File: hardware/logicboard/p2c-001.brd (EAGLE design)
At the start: 89 x 51 mm, 53 parts, among them IC1 74LS06N, J1 MKR, J11 Qwiic, J2 GPIO, J3 9V, J4 RLY, J5 SPI, J6 DIN5, J7 DIN5, K1 G5V1, Q11 220mA/50V/3.5Ω, Q12 220mA/50V/3.5Ω, T1 2SC1815, U1 DS18B20

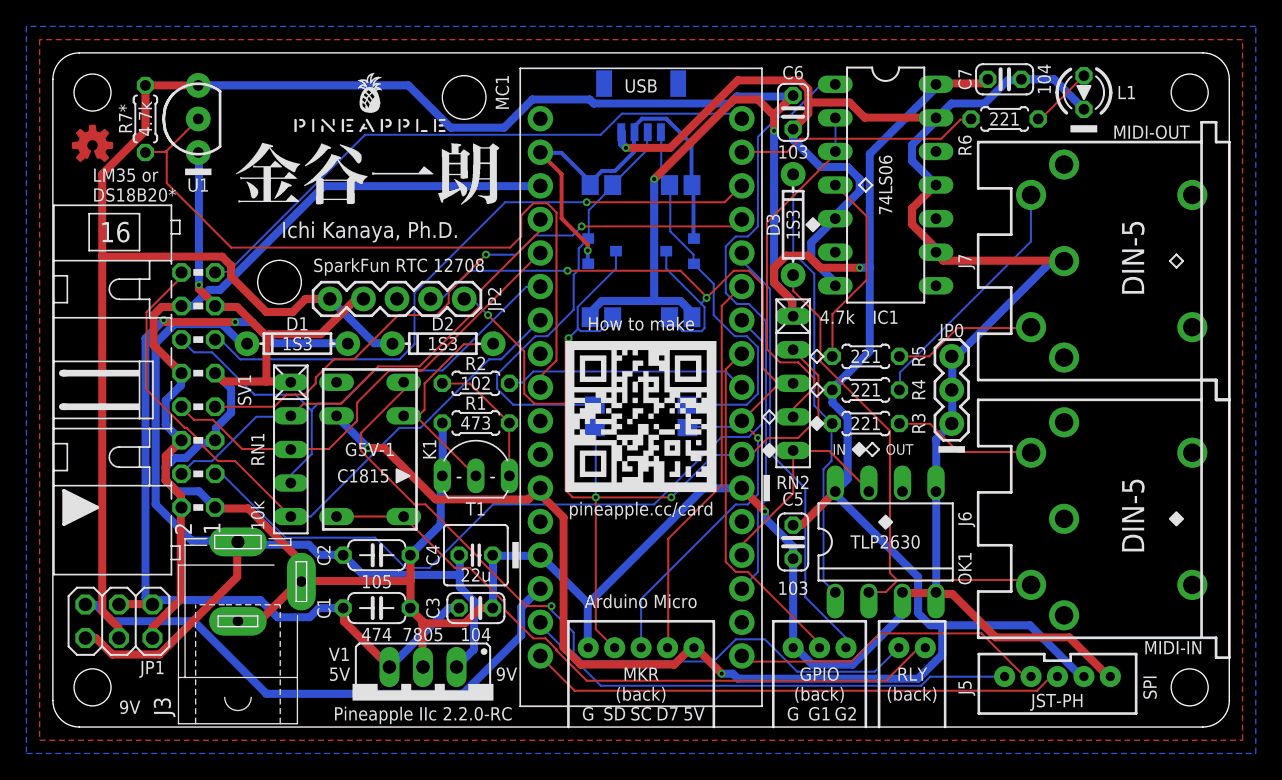
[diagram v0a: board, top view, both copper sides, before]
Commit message: Renumbered pins.
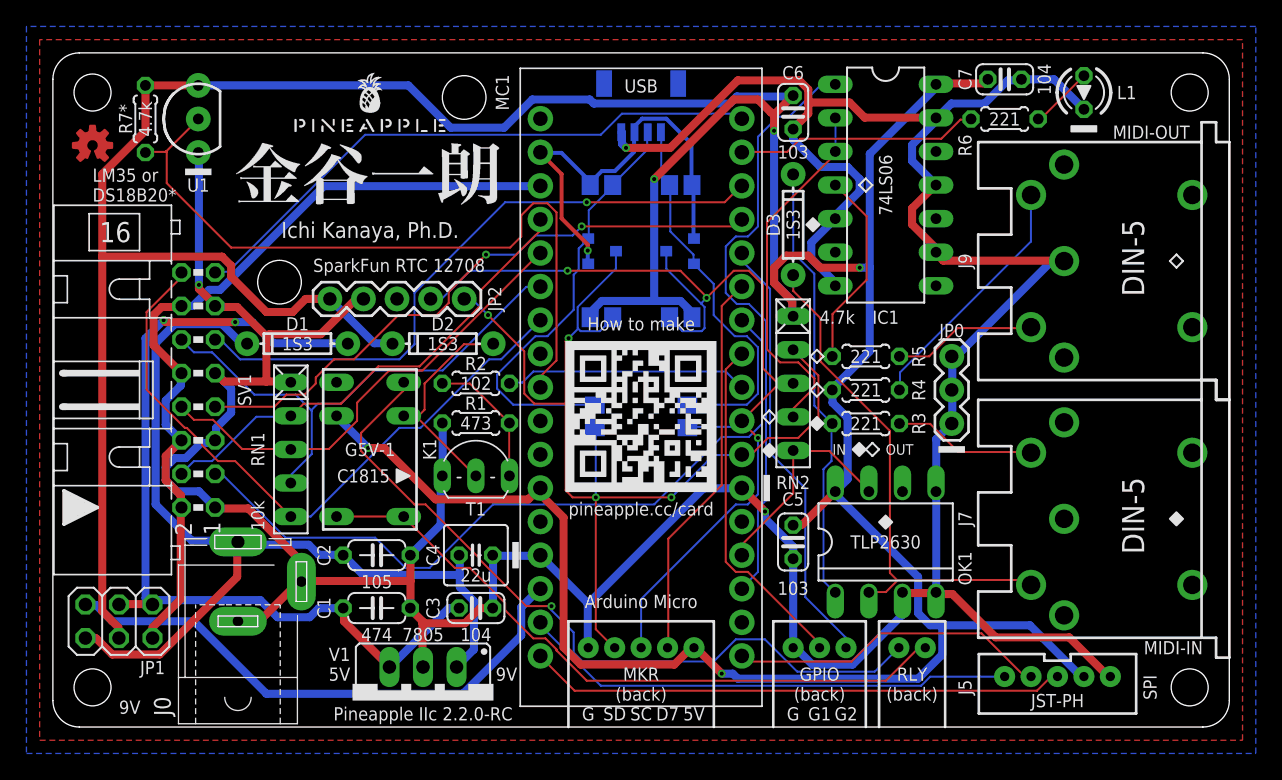
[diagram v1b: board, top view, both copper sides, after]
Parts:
- removed J6: DIN5, SparkFun-Connectors:DIN5-RA-PTH
- added J9: DIN5, SparkFun-Connectors:DIN5-RA-PTH
- moved J7 19.5 mm to (89.0, 15.8)
- renumbered J3 to J0
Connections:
- net GND: now also J9.2; no longer J7.2
- net MIRTN: now also J7.5; no longer J6.5
- net MISND: now also J7.4; no longer J6.4
- net MORTN: now also J9.5; no longer J7.5
- net MOSND: now also J9.4; no longer J7.4
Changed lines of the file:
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@@
 <element name="U$1" library="pineapple" package="PINEAPPLE450_SILK" value="PINEAPPLE450_SILK" x="24" y="45" smashed="yes"/>
 <element name="U$2" library="adafruit" package="ARDUINOMICRO" value="ARDUINOMICRO" x="44.5" y="25.7" smashed="yes" rot="R270"/>
-<element name="J7" library="SparkFun-Connectors" library_urn="urn:adsk.eagle:library:513" package="DIN5-RA-PTH" package3d_urn="urn:adsk.eagle:package:38294/1" value="DIN5" x="89" y="35.25" smashed="yes" rot="R90">
+<element name="J9" library="SparkFun-Connectors" library_urn="urn:adsk.eagle:library:513" package="DIN5-RA-PTH" package3d_urn="urn:adsk.eagle:package:38294/1" value="DIN5" x="89" y="35.25" smashed="yes" rot="R90">
 <attribute name="NAME" x="69.5" y="35.25" size="1" layer="25" ratio="20" rot="R90" align="bottom-center"/>
 <attribute name="PROD_ID" value="CONN-09481" x="89" y="35.25" size="1.778" layer="27" rot="R90" display="off"/>
 <attribute name="VALUE" x="85.063" y="33.98" size="0.6096" layer="27" font="vector" ratio="20" rot="R90"/>
 </element>
-<element name="J6" library="SparkFun-Connectors" library_urn="urn:adsk.eagle:library:513" package="DIN5-RA-PTH" package3d_urn="urn:adsk.eagle:package:38294/1" value="DIN5" x="89" y="15.75" smashed="yes" rot="R90">
+<element name="J7" library="SparkFun-Connectors" library_urn="urn:adsk.eagle:library:513" package="DIN5-RA-PTH" package3d_urn="urn:adsk.eagle:package:38294/1" value="DIN5" x="89" y="15.75" smashed="yes" rot="R90">
 <attribute name="NAME" x="69.5" y="15.75" size="1" layer="25" ratio="20" rot="R90" align="bottom-center"/>
 <attribute name="PROD_ID" value="CONN-09481" x="89" y="15.75" size="1.778" layer="27" rot="R90" display="off"/>
@@
 <attribute name="VALUE" x="56.349" y="3.46" size="0.6096" layer="28" font="vector" ratio="20" rot="MR180"/>
 </element>
-<element name="J3" library="con-jack" library_urn="urn:adsk.eagle:library:154" package="SPC4077" package3d_urn="urn:adsk.eagle:package:7492/1" value="9V" x="14" y="11" smashed="yes" rot="R90">
+<element name="J0" library="con-jack" library_urn="urn:adsk.eagle:library:154" package="SPC4077" package3d_urn="urn:adsk.eagle:package:7492/1" value="9V" x="14" y="11" smashed="yes" rot="R90">
 <attribute name="MF" value="" x="14" y="11" size="1.778" layer="27" rot="R90" display="off"/>
 <attribute name="MPN" value="" x="14" y="11" size="1.778" layer="27" rot="R90" display="off"/>
@@
 <signal name="GND" class="1">
 <contactref element="IC1" pad="7"/>
-<contactref element="J7" pad="2"/>
+<contactref element="J9" pad="2"/>
 <contactref element="IC1" pad="13"/>
 <contactref element="IC1" pad="11"/>
@@
 <contactref element="J2" pad="1"/>
 <contactref element="J1" pad="1"/>
-<contactref element="J3" pad="2"/>
-<contactref element="J3" pad="1"/>
+<contactref element="J0" pad="2"/>
+<contactref element="J0" pad="1"/>
 <contactref element="JP2" pad="2"/>
 <contactref element="J5" pad="1"/>
@@
 <signal name="MIRTN">
 <contactref element="D3" pad="A"/>
-<contactref element="J6" pad="5"/>
+<contactref element="J7" pad="5"/>
 <contactref element="OK1" pad="2"/>
 <wire x1="63.0174" y1="10.2108" x2="61.7982" y2="10.2108" width="0.1524" layer="1"/>
@@
 <signal name="MISND">
 <contactref element="R3" pad="2"/>
-<contactref element="J6" pad="4"/>
+<contactref element="J7" pad="4"/>
 <wire x1="66.3702" y1="22.9362" x2="64.0842" y2="22.9362" width="0.1524" layer="1"/>
 <wire x1="68.5038" y1="20.8026" x2="66.3702" y2="22.9362" width="0.1524" layer="1"/>
@@
 <signal name="MOSND">
 <contactref element="R4" pad="2"/>
-<contactref element="J7" pad="4"/>
+<contactref element="J9" pad="4"/>
 <wire x1="64.0842" y1="26.8224" x2="64.0842" y2="25.527" width="0.1524" layer="16"/>
 <wire x1="73.9902" y1="36.7284" x2="64.0842" y2="26.8224" width="0.1524" layer="16"/>
@@
 <signal name="MORTN">
 <contactref element="R5" pad="2"/>
-<contactref element="J7" pad="5"/>
+<contactref element="J9" pad="5"/>
 <wire x1="66.294" y1="28.0416" x2="64.0842" y2="28.0416" width="0.1524" layer="1"/>
 <wire x1="68.4276" y1="30.1752" x2="66.294" y2="28.0416" width="0.1524" layer="1"/>
@@
 <contactref element="C4" pad="1"/>
 <contactref element="V1" pad="IN"/>
-<contactref element="J3" pad="3"/>
+<contactref element="J0" pad="3"/>
 <contactref element="JP1" pad="1"/>
 <wire x1="30.7848" y1="10.5918" x2="30.7848" y2="11.5062" width="0.6096" layer="16"/>

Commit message: Renumbered parts.
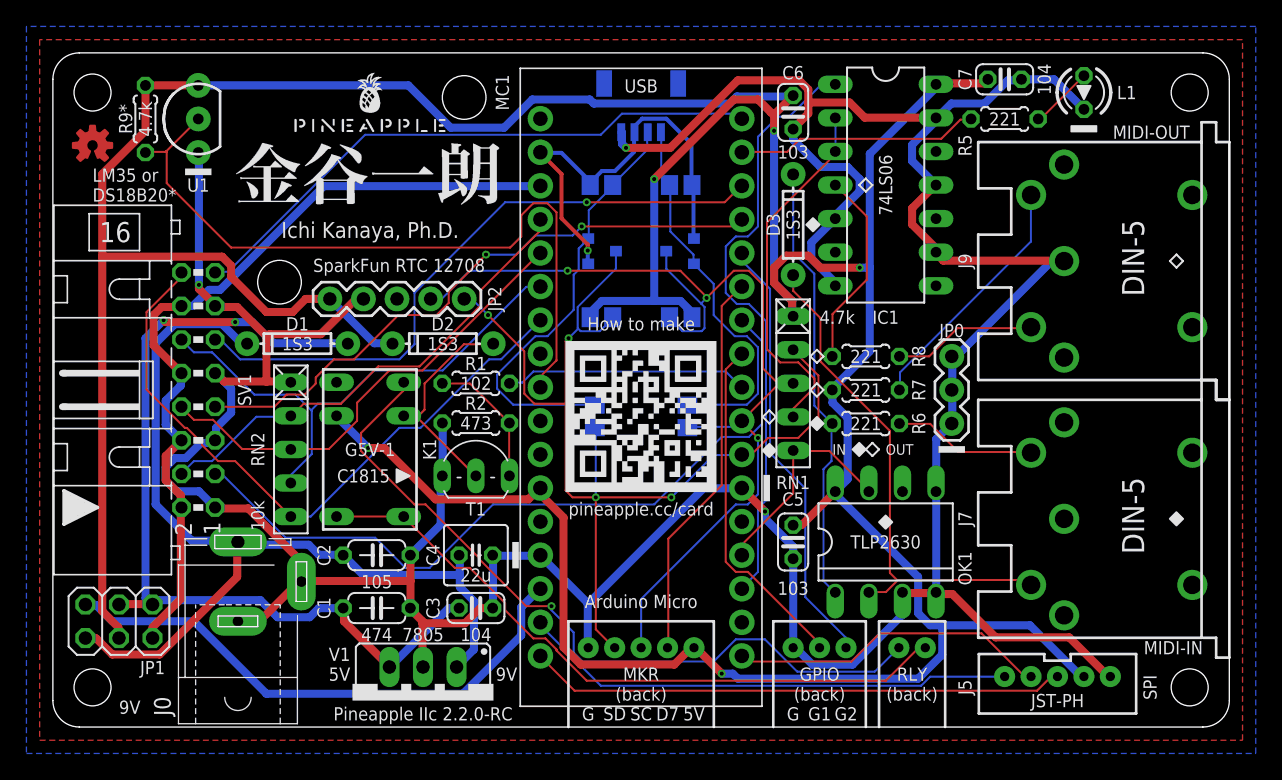
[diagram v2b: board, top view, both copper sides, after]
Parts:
- removed R3: 220, resistor:0204/5
- added R8: 220, resistor:0204/5
- R1: value 47k -> 1k
- R2: value 1k -> 47k
- RN1: value 10k -> 4.7k
- RN2: value 4.7k -> 10k
- moved RN1 38.3 mm to (56.0, 26.0)
- moved RN2 38.3 mm to (18.0, 21.0)
- moved R6 25.3 mm to (61.5, 23.0), turned to 0 degrees
- moved R5 20.8 mm to (72.0, 46.0), turned to 180 degrees
- moved R1 3.00 mm to (32.0, 26.0)
- moved R2 3.00 mm to (32.0, 23.0)
- renumbered R11 to R201, R12 to R202, R13 to R203, R14 to R204, R4 to R7, R7* to R9*
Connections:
- net ANLG1: now also RN2.2; no longer RN1.2
- net ANLG2: now also RN2.3; no longer RN1.3
- net ANLG3: now also RN2.4; no longer RN1.4
- net ANLG4: now also RN2.5; no longer RN1.5
- net GND: now also R2.1, RN2.1; no longer R1.1, RN1.1
- net LED1: now also R5.2; no longer R6.2
- net LED1A: now also R5.1; no longer R6.1
- net MIA: now also R6.1; no longer R3.1
- net MISND: now also R6.2; no longer R3.2
- net MORTN: now also R8.2; no longer R5.2
- net MORTNRAW: now also R8.1; no longer R5.1
- net NMORTN: now also RN1.4; no longer RN2.4
- net RLY: now also R1.2; no longer R2.2
- net RLYQ: now also R1.1, R2.2; no longer R1.2, R2.1
- net RX: now also RN1.5; no longer RN2.5
- net SCL: now also RN1.3; no longer RN2.3
- net SDA: now also RN1.2; no longer RN2.2
- net VCC: now also RN1.1; no longer RN2.1
